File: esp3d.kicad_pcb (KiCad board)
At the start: 2 copper layers, 36.2 x 34.9 mm, 12 parts, among them J1 PROG, U1 LM1117-3.3, U2 ESP-12E

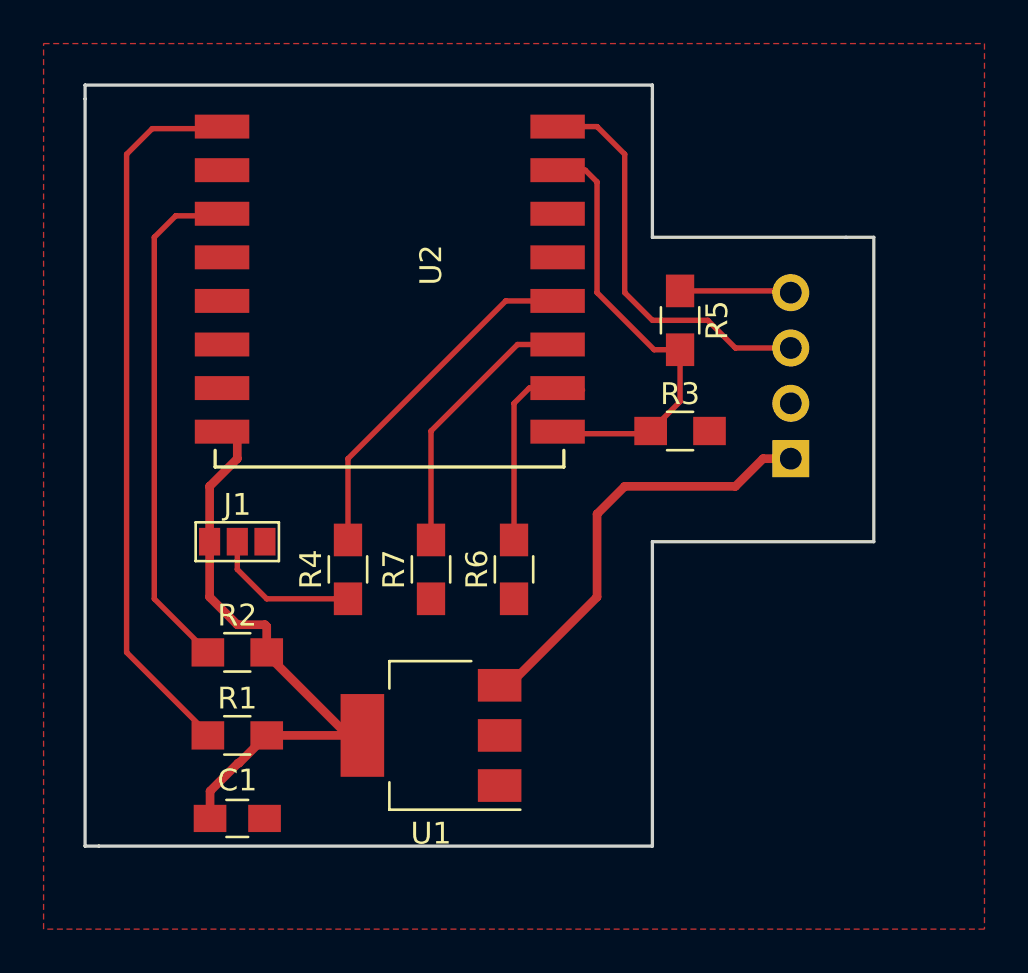
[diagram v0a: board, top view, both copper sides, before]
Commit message: Reversed the ramps connector. Removed resistors that may have prevented programming
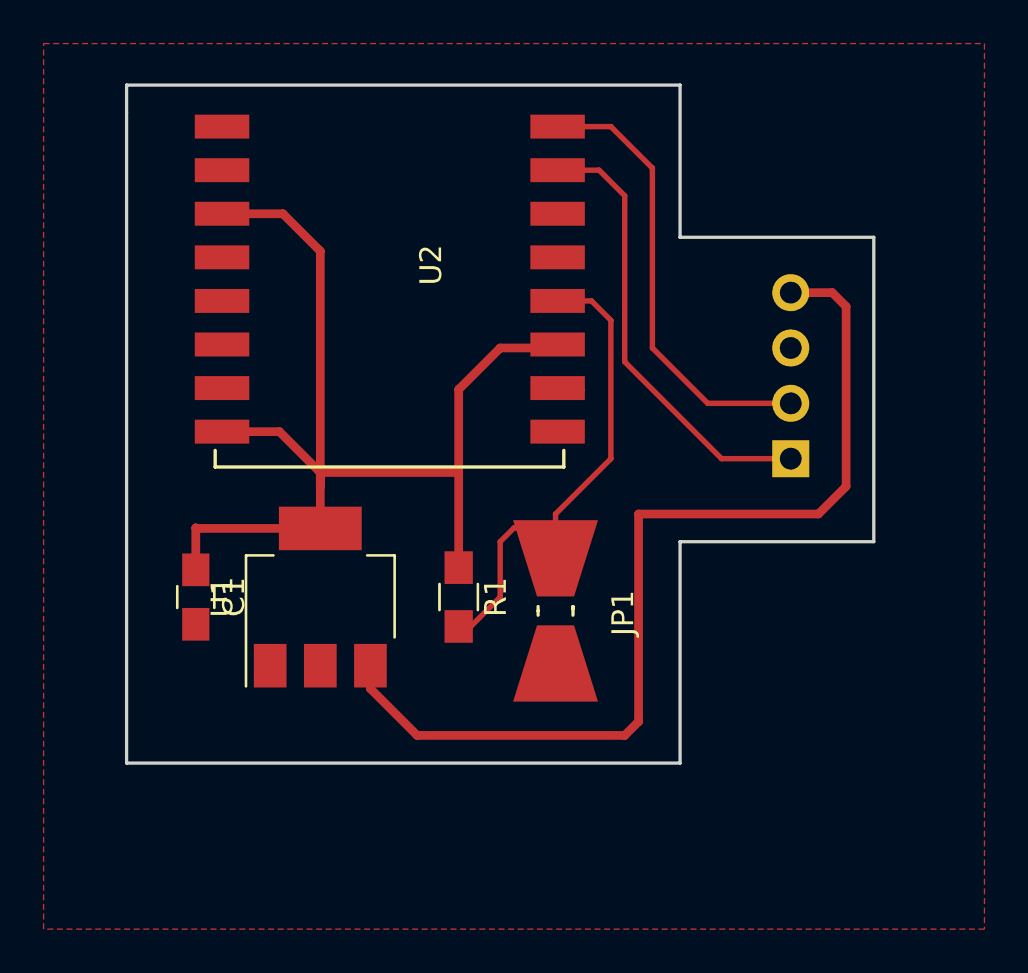
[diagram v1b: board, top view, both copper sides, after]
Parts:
- removed J1: PROG, Connectors:GS3
- removed R2, R4: 10k, Resistors_SMD:R_0805_HandSoldering
- removed R3: 2k, Resistors_SMD:R_0805_HandSoldering
- removed R5, R6, R7: 1k, Resistors_SMD:R_0805_HandSoldering
- added JP1: Jumper, Resistors_Universal:Resistor_SMDuniversal_0805to2512_HandSoldering, F.Cu at (184.8, 137.8)
- R1: value 10k -> R
- RAMPS1: value Conn_01x04_Female -> (none)
- moved R1 12.0 mm to (180.3, 137.2), turned to 270 degrees
- moved C1 10.3 mm to (168.3, 137.2), turned to 270 degrees
- moved U1 8.13 mm to (174.0, 137.2), turned to 90 degrees
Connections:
- R1 pad 1: Net-(R1-Pad1) -> +3V3
- R1 pad 2: +3V3 -> PROG
- RAMPS1 pad 1: +5V -> TX
- RAMPS1 pad 2: GND -> RX
- RAMPS1 pad 3: RX -> GND
- RAMPS1 pad 4: Net-(R5-Pad1) -> +5V
- U2 pad 1: Net-(R1-Pad1) -> (no net)
- U2 pad 10: Net-(R6-Pad2) -> GND
- U2 pad 11: Net-(R7-Pad2) -> +3V3
- U2 pad 13: Net-(U2-Pad13) -> (no net)
- U2 pad 14: Net-(U2-Pad14) -> (no net)
- U2 pad 2: Net-(U2-Pad2) -> (no net)
- U2 pad 3: Net-(R2-Pad1) -> +3V3
- U2 pad 4: Net-(U2-Pad4) -> (no net)
- U2 pad 5: Net-(U2-Pad5) -> (no net)
- U2 pad 6: Net-(U2-Pad6) -> (no net)
- U2 pad 7: Net-(U2-Pad7) -> (no net)
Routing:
- net Net-(R1-Pad1): track 32.9 -> 0.00 mm
- net +5V: track 20.3 -> 45.3 mm
- net Net-(R2-Pad1): track 23.4 -> 0.00 mm
- net +3V3: track 30.0 -> 49.3 mm
- net Net-(R7-Pad2): track 11.8 -> 0.00 mm
- net Net-(R6-Pad2): track 9.42 -> 0.00 mm
- net PROG: track 15.6 -> 23.9 mm
- net Net-(J1-Pad2): track 6.91 -> 0.00 mm
- net Net-(R5-Pad1): track 5.23 -> 0.00 mm
- net TX: track 17.2 -> 21.3 mm
- net GND: track 4.94 -> 1.56 mm
- net RX: track 19.3 -> 21.5 mm
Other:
- board size 36.2 x 34.9 mm -> 34.3 x 31.1 mm
